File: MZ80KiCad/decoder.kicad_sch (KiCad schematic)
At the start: 10 parts, among them U30 74LS42, U47 74154, U53 74S157, U54 74LS04, U56 74S157, U57 74150, U58 74LS00

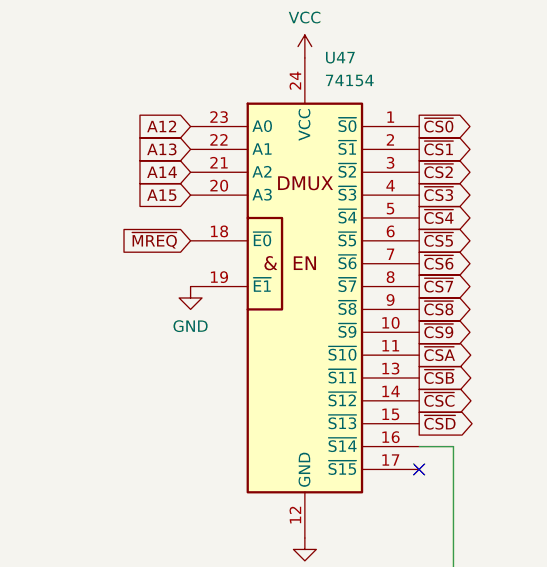
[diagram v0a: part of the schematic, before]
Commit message: fix U47 pin18 pin19
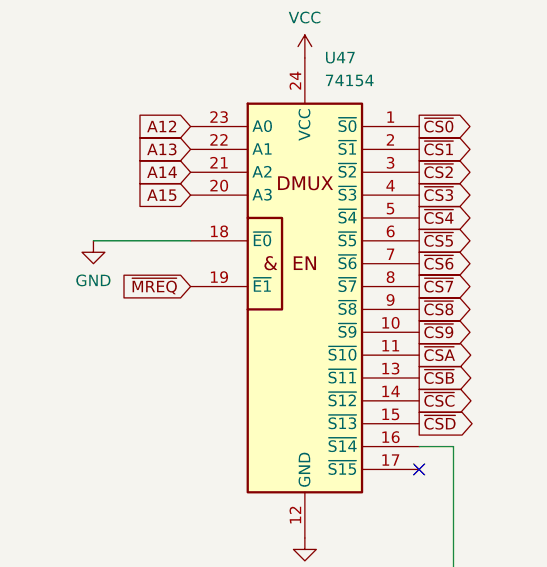
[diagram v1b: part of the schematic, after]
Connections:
- net GND: now also U47.18 (~{E0}); no longer U47.19 (~{E1})
- net ~{MREQ}: now also U47.19 (~{E1}); no longer U47.18 (~{E0})
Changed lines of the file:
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@@
+    (stroke (width 0) (type default))
+  )
+  (wire (pts (xy 24.765 97.155) (xy 35.56 97.155))
     (stroke (width 0) (type default))
   )
@@
     )
   )
-  (global_label "~{MREQ}" (shape input) (at 35.56 97.155 180) (fields_autoplaced)
-    (effects (font (size 1.27 1.27)) (justify right))
-    (property "Intersheetrefs" "${INTERSHEET_REFS}" (at 27.3739 97.155 0)
+  (global_label "~{MREQ}" (shape input) (at 35.56 102.235 180) (fields_autoplaced)
+    (effects (font (size 1.27 1.27)) (justify right))
+    (property "Intersheetrefs" "${INTERSHEET_REFS}" (at 27.3739 102.235 0)
       (effects (font (size 1.27 1.27)) (justify right) hide)
     )
@@
     )
   )
-  (symbol (lib_id "power:GND") (at 35.56 102.235 0) (unit 1)
-    (in_bom yes) (on_board yes) (dnp no) (fields_autoplaced)
-    (property "Reference" "#PWR034" (at 35.56 108.585 0)
-      (effects (font (size 1.27 1.27)) hide)
-    )
-    (property "Value" "GND" (at 35.56 106.68 0)
-      (effects (font (size 1.27 1.27)))
-    )
-    (property "Footprint" "" (at 35.56 102.235 0)
-      (effects (font (size 1.27 1.27)) hide)
-    )
-    (property "Datasheet" "" (at 35.56 102.235 0)
-      (effects (font (size 1.27 1.27)) hide)
-    )
+  (symbol (lib_id "power:GND") (at 24.765 97.155 0) (unit 1)
+    (in_bom yes) (on_board yes) (dnp no) (fields_autoplaced)
+    (property "Reference" "#PWR034" (at 24.765 103.505 0)
+      (effects (font (size 1.27 1.27)) hide)
+    )
+    (property "Value" "GND" (at 24.765 101.6 0)
+      (effects (font (size 1.27 1.27)))
+    )
+    (property "Footprint" "" (at 24.765 97.155 0)
+      (effects (font (size 1.27 1.27)) hide)
+    )
+    (property "Datasheet" "" (at 24.765 97.155 0)
+      (effects (font (size 1.27 1.27)) hide)
+    )
